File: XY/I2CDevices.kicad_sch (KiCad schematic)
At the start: 32 parts, among them U1 OPT4003DNPRQ1, U10 NCV891330PD50R2G, U2 ADM1176-1ARMZ-R7, U5 DRV8830DRC, U6 ADM1176-1ARMZ-R7

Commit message: Z- Solar Panel files upload
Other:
- note added: "I2C ADDR 0x4A Install R95: 0x48"
- note removed: "I2C ADDR 0x94 Install R95: 0x90"
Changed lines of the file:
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@@
 		)
 	)
-	(text "I2C ADDR\n0x94\nInstall R95: 0x90"
+	(text "I2C ADDR\n0x4A\nInstall R95: 0x48"
 		(exclude_from_sim no)
 		(at 72.898 116.586 0)

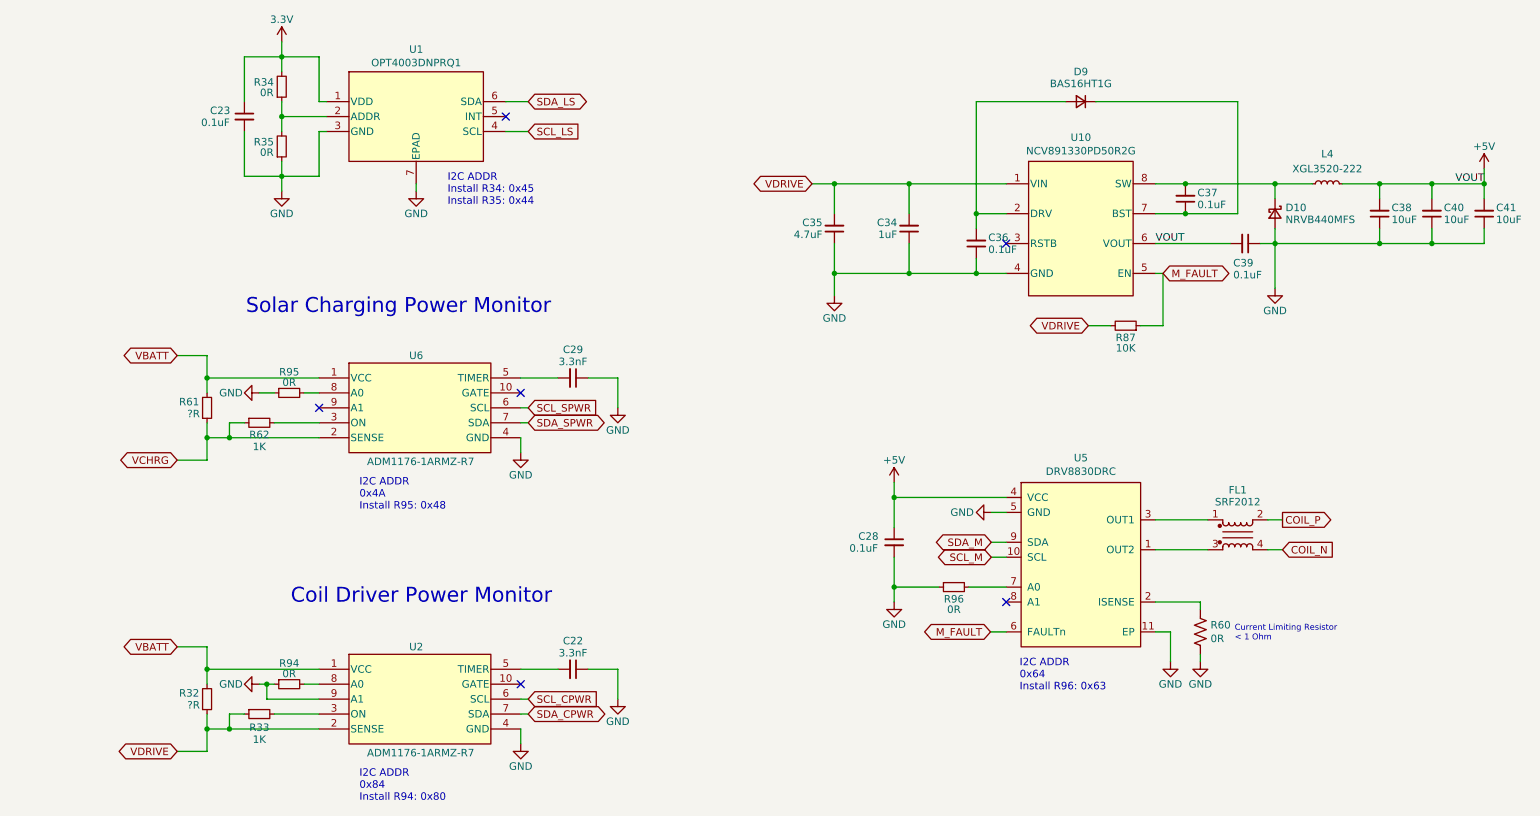
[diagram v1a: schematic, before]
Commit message: Added address breakouts
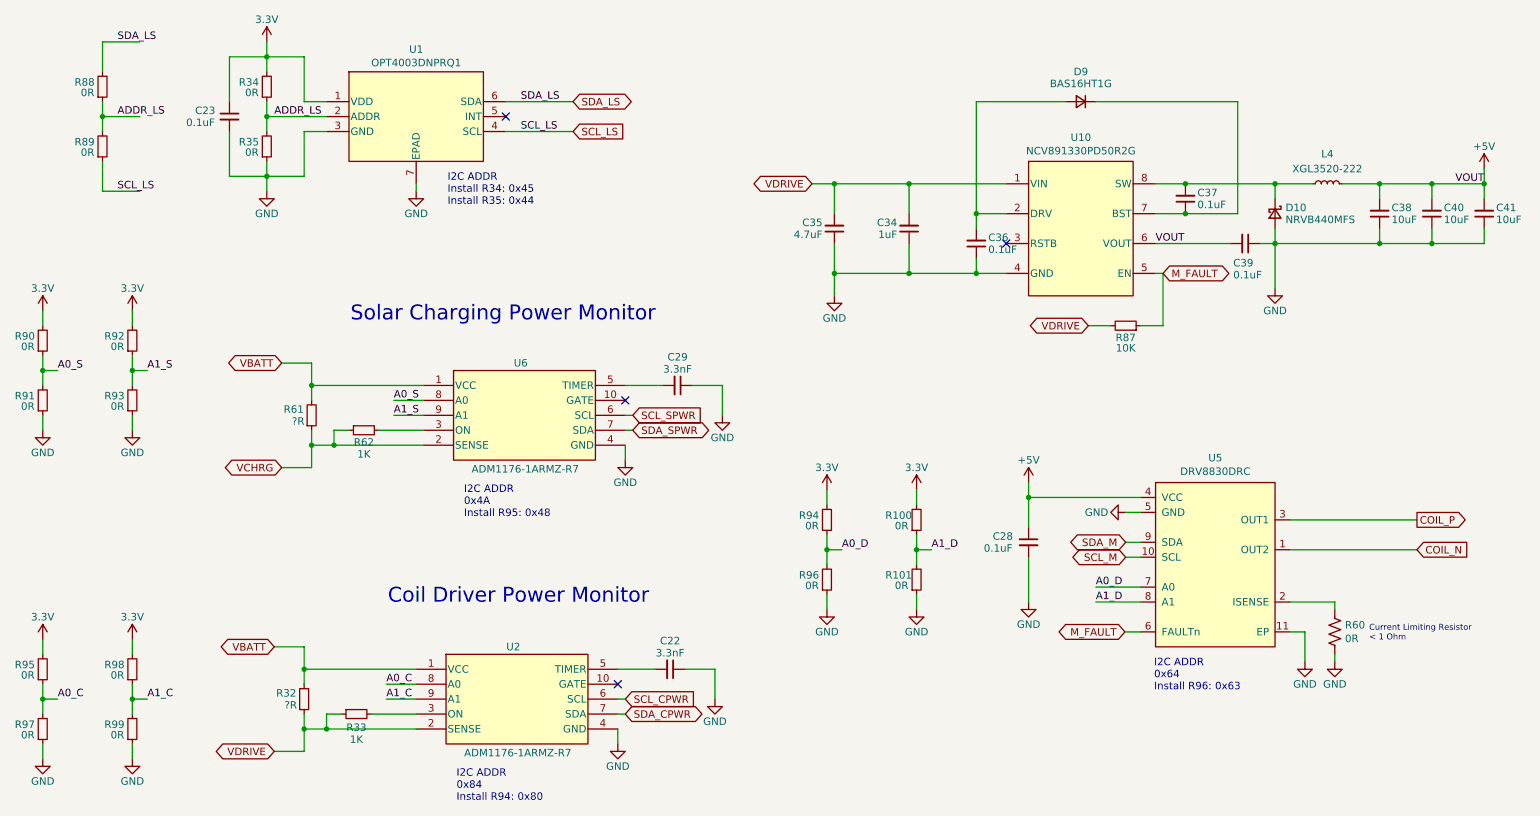
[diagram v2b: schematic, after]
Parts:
- removed FL1: SRF2012, SolarPanels:SRF2012, symbol Device:Filter_EMI_CommonMode
- added R100, R101, R88, R89, R90, R91, R92, R93, R97, R98, R99: 0R, Resistor_SMD:R_0603_1608Metric, symbol Device:R_Small
- C23: footprint Capacitor_SMD:C_0402_1005Metric -> Capacitor_SMD:C_0603_1608Metric
- R34, R35: footprint Resistor_SMD:R_0402_1005Metric -> Resistor_SMD:R_0603_1608Metric
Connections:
- net 3.3V: now also R94.2, R95.2, R100.2, R90.2, R92.2, R98.2
- net COIL_N: now also U5.1 (OUT2)
- net COIL_P: now also U5.3 (OUT1)
- net GND: now also R101.1, R91.1, R93.1, R97.1, R99.1; no longer R94.1, R95.1, U2.9 (A1)
- net SCL_LS: now also R89.1
- net SDA_LS: now also R88.2
- net ADDR_LS: now reaches R34.1, R35.2, U1.2 (ADDR)
- net ADDR_LS: now also R88.1, R89.2
- net A0_D: now reaches R96.2, U5.7 (A0)
- net A0_D: now also R94.1
- net A1_D: now reaches U5.8 (A1)
- net A1_D: now also R100.1, R101.2
- net A0_S: now reaches U6.8 (A0)
- net A0_S: now also R90.1, R91.2; no longer R95.2
- net A1_S: now reaches U6.9 (A1)
- net A1_S: now also R92.1, R93.2
- net A0_C: now reaches U2.8 (A0)
- net A0_C: now also R95.1, R97.2; no longer R94.2
- new net A1_C: R98.1, R99.2, U2.9 (A1)
- no-connect marks 6 -> 4
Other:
- moved on the sheet: C22, C23, C28, C29, R32, R33, R34, R35, R60, R61, R62, U2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
